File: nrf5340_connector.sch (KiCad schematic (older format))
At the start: 0 parts

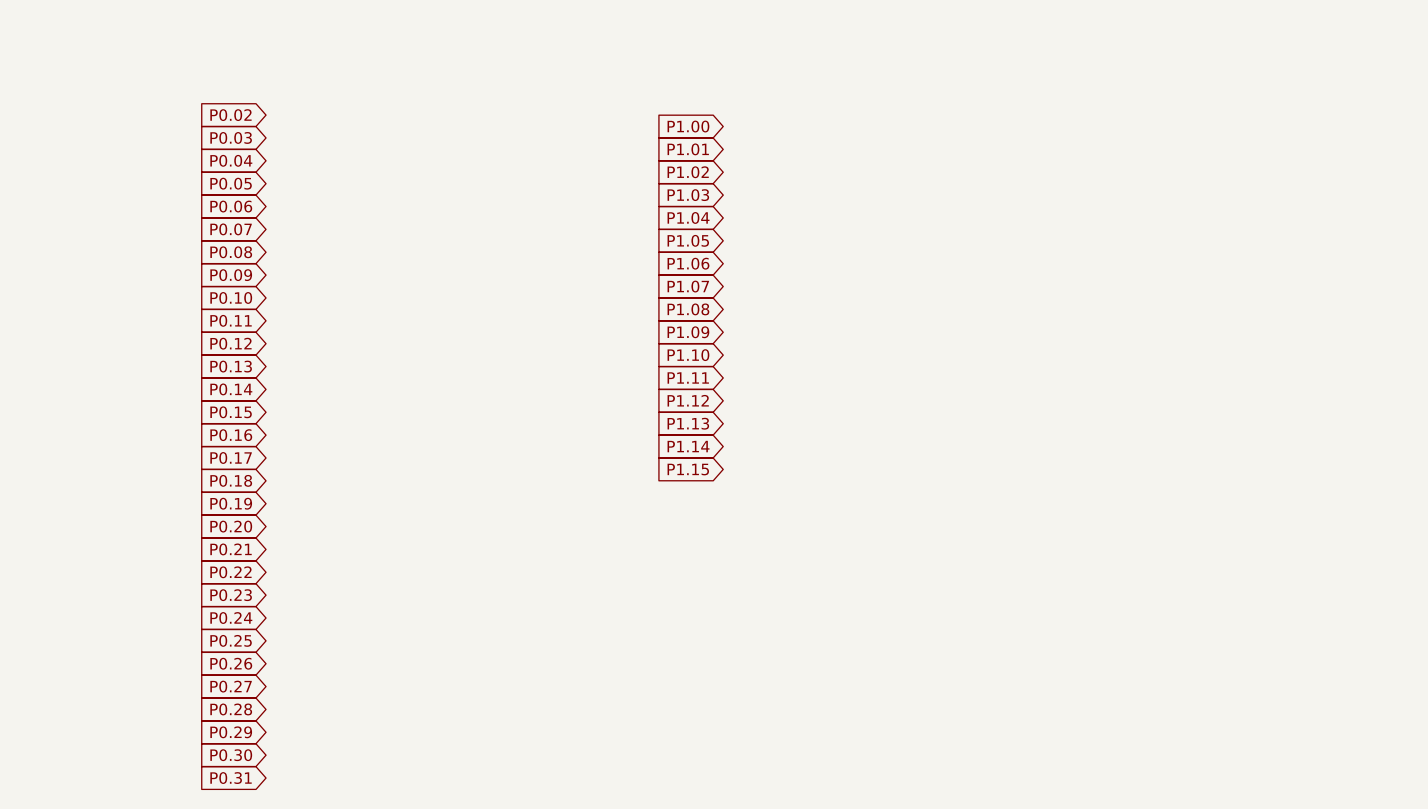
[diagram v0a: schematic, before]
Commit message: first rev pcb without impedance matching
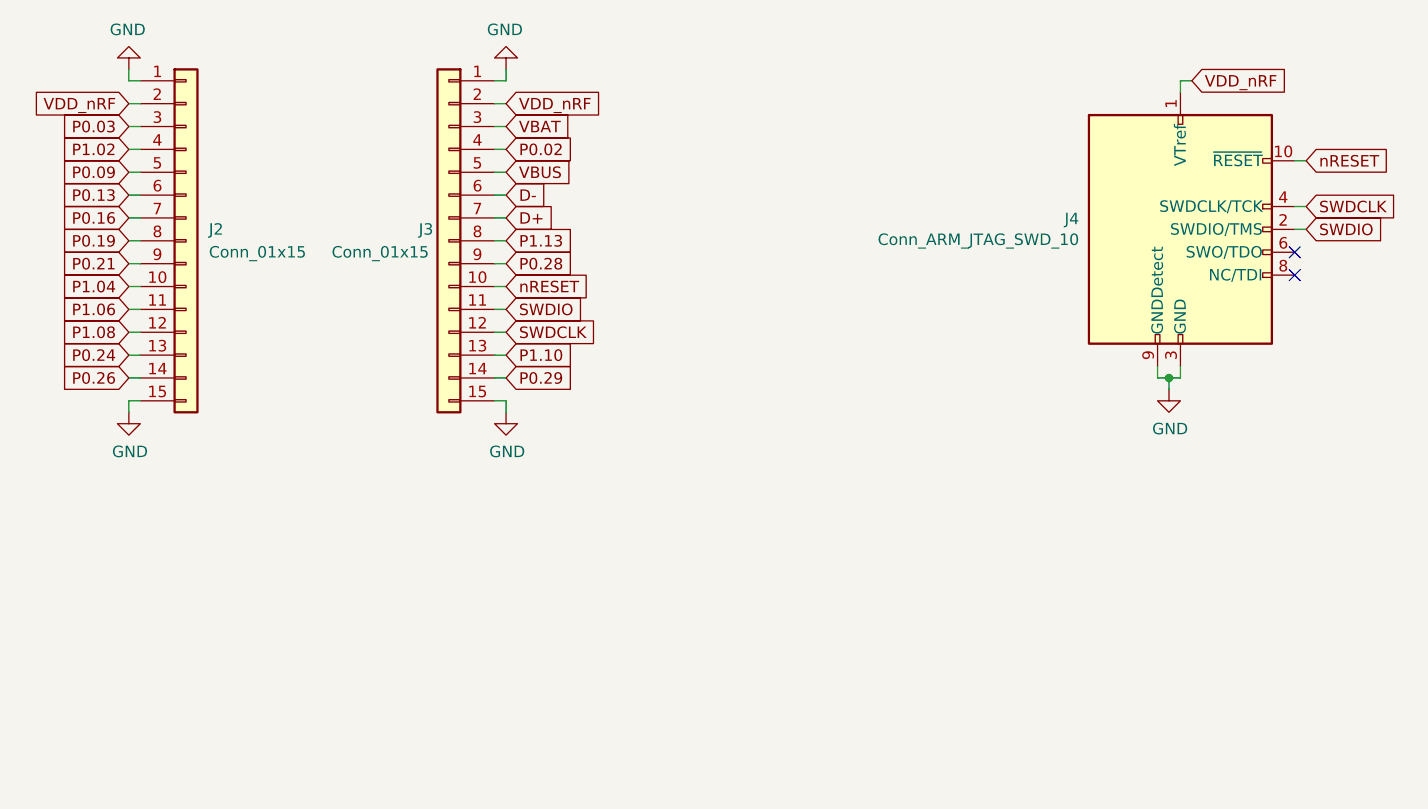
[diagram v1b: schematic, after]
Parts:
- added J2, J3: Conn_01x15, Connector_PinHeader_1.27mm:PinHeader_1x15_P1.27mm_Vertical, symbol Connector_Generic:Conn_01x15
- added J4: Conn_ARM_JTAG_SWD_10, Connector_PinHeader_1.27mm:PinHeader_2x05_P1.27mm_Vertical_SMD, symbol Connector:Conn_ARM_JTAG_SWD_10
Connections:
- net P0.02: now also J3.4 (Pin_4)
- net P0.03: now also J2.3 (Pin_3)
- net P0.09: now also J2.5 (Pin_5)
- net P0.13: now also J2.6 (Pin_6)
- net P0.16: now also J2.7 (Pin_7)
- net P0.19: now also J2.8 (Pin_8)
- net P0.21: now also J2.9 (Pin_9)
- net P0.24: now also J2.13 (Pin_13)
- net P0.26: now also J2.14 (Pin_14)
- net P0.28: now also J3.9 (Pin_9)
- net P0.29: now also J3.14 (Pin_14)
- net P1.02: now also J2.4 (Pin_4)
- net P1.04: now also J2.10 (Pin_10)
- net P1.06: now also J2.11 (Pin_11)
- net P1.08: now also J2.12 (Pin_12)
- net P1.10: now also J3.13 (Pin_13)
- net P1.13: now also J3.8 (Pin_8)
- new net D+: J3.7 (Pin_7)
- new net D-: J3.6 (Pin_6)
- new net GND: J2.1 (Pin_1), J2.15 (Pin_15), J3.1 (Pin_1), J3.15 (Pin_15), J4.3 (GND), J4.5 (GND), J4.9 (GNDDetect)
- new net SWDCLK: J3.12 (Pin_12), J4.4 (SWDCLK/TCK)
- new net SWDIO: J3.11 (Pin_11), J4.2 (SWDIO/TMS)
- new net VBAT: J3.3 (Pin_3)
- new net VBUS: J3.5 (Pin_5)
- new net VDD_nRF: J2.2 (Pin_2), J3.2 (Pin_2), J4.1 (VTref)
- new net nRESET: J3.10 (Pin_10), J4.10 (~RESET~)
- no-connect marks 0 -> 2

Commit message: fix traces underneath nrf gnd pad and VDD_HV
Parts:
- renumbered J4 to J?, J2 to J?, J3 to J?
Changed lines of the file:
@@
 EESchema Schematic File Version 4
+LIBS:nrf5340_module-cache
 EELAYER 30 0
 EELAYER END
@@
 P1.13
 $Comp
-L Connector:Conn_ARM_JTAG_SWD_10 J4
+L Connector:Conn_ARM_JTAG_SWD_10 J?
 U 1 1 5E0665C6
 P 5500 1400
-F 0 "J4" H 5057 1446 50  0000 R CNN
+F 0 "J?" H 5057 1446 50  0000 R CNN
 F 1 "Conn_ARM_JTAG_SWD_10" H 5057 1355 50  0000 R CNN
 F 2 "Connector_PinHeader_1.27mm:PinHeader_2x05_P1.27mm_Vertical_SMD" H 5500 1400 50  0001 C CNN
@@
 VDD_nRF
 $Comp
-L power:GND #PWR0123
+L power:GND #PWR?
 U 1 1 5E077D9A
 P 900 700
-F 0 "#PWR0123" H 900 450 50  0001 C CNN
+F 0 "#PWR?" H 900 450 50  0001 C CNN
 F 1 "GND" H 905 527 50  0000 C CNN
 F 2 "" H 900 700 50  0001 C CNN
@@
 $EndComp
 $Comp
-L power:GND #PWR0124
+L power:GND #PWR?
 U 1 1 5E0780C3
 P 900 2200
-F 0 "#PWR0124" H 900 1950 50  0001 C CNN
+F 0 "#PWR?" H 900 1950 50  0001 C CNN
 F 1 "GND" H 905 2027 50  0000 C CNN
 F 2 "" H 900 2200 50  0001 C CNN
@@
 $EndComp
 $Comp
-L power:GND #PWR0127
+L power:GND #PWR?
 U 1 1 5E078950
 P 2550 2200
-F 0 "#PWR0127" H 2550 1950 50  0001 C CNN
+F 0 "#PWR?" H 2550 1950 50  0001 C CNN
 F 1 "GND" H 2555 2027 50  0000 C CNN
 F 2 "" H 2550 2200 50  0001 C CNN
@@
 $EndComp
 $Comp
-L power:GND #PWR0128
+L power:GND #PWR?
 U 1 1 5E07908A
 P 2550 700
-F 0 "#PWR0128" H 2550 450 50  0001 C CNN
+F 0 "#PWR?" H 2550 450 50  0001 C CNN
 F 1 "GND" H 2555 527 50  0000 C CNN
 F 2 "" H 2550 700 50  0001 C CNN
@@
 $EndComp
 $Comp
-L power:GND #PWR0129
+L power:GND #PWR?
 U 1 1 5E07B32C
 P 5450 2100
-F 0 "#PWR0129" H 5450 1850 50  0001 C CNN
+F 0 "#PWR?" H 5450 1850 50  0001 C CNN
 F 1 "GND" H 5455 1927 50  0000 C CNN
 F 2 "" H 5450 2100 50  0001 C CNN
@@
 	900  700  900  750
 $Comp
-L Connector_Generic:Conn_01x15 J2
+L Connector_Generic:Conn_01x15 J?
 U 1 1 5E152486
 P 1150 1450
-F 0 "J2" H 1250 1500 50  0000 L CNN
+F 0 "J?" H 1250 1500 50  0000 L CNN
 F 1 "Conn_01x15" H 1250 1400 50  0000 L CNN
 F 2 "Connector_PinHeader_1.27mm:PinHeader_1x15_P1.27mm_Vertical" H 1150 1450 50  0001 C CNN
@@
 	950  850  900  850
 $Comp
-L Connector_Generic:Conn_01x15 J3
+L Connector_Generic:Conn_01x15 J?
 U 1 1 5E15CBB6
 P 2300 1450
-F 0 "J3" H 2400 1500 50  0000 C CNN
+F 0 "J?" H 2400 1500 50  0000 C CNN
 F 1 "Conn_01x15" H 2600 1400 50  0000 C CNN
 F 2 "Connector_PinHeader_1.27mm:PinHeader_1x15_P1.27mm_Vertical" H 2300 1450 50  0001 C CNN

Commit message: fix vdd_hv
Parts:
- gave numbers to parts that had none: 3
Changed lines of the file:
@@
 P1.13
 $Comp
-L Connector:Conn_ARM_JTAG_SWD_10 J?
+L Connector:Conn_ARM_JTAG_SWD_10 J4
 U 1 1 5E0665C6
 P 5500 1400
-F 0 "J?" H 5057 1446 50  0000 R CNN
+F 0 "J4" H 5057 1446 50  0000 R CNN
 F 1 "Conn_ARM_JTAG_SWD_10" H 5057 1355 50  0000 R CNN
 F 2 "Connector_PinHeader_1.27mm:PinHeader_2x05_P1.27mm_Vertical_SMD" H 5500 1400 50  0001 C CNN
@@
 VDD_nRF
 $Comp
-L power:GND #PWR?
+L power:GND #PWR0123
 U 1 1 5E077D9A
 P 900 700
-F 0 "#PWR?" H 900 450 50  0001 C CNN
+F 0 "#PWR0123" H 900 450 50  0001 C CNN
 F 1 "GND" H 905 527 50  0000 C CNN
 F 2 "" H 900 700 50  0001 C CNN
@@
 $EndComp
 $Comp
-L power:GND #PWR?
+L power:GND #PWR0124
 U 1 1 5E0780C3
 P 900 2200
-F 0 "#PWR?" H 900 1950 50  0001 C CNN
+F 0 "#PWR0124" H 900 1950 50  0001 C CNN
 F 1 "GND" H 905 2027 50  0000 C CNN
 F 2 "" H 900 2200 50  0001 C CNN
@@
 $EndComp
 $Comp
-L power:GND #PWR?
+L power:GND #PWR0127
 U 1 1 5E078950
 P 2550 2200
-F 0 "#PWR?" H 2550 1950 50  0001 C CNN
+F 0 "#PWR0127" H 2550 1950 50  0001 C CNN
 F 1 "GND" H 2555 2027 50  0000 C CNN
 F 2 "" H 2550 2200 50  0001 C CNN
@@
 $EndComp
 $Comp
-L power:GND #PWR?
+L power:GND #PWR0128
 U 1 1 5E07908A
 P 2550 700
-F 0 "#PWR?" H 2550 450 50  0001 C CNN
+F 0 "#PWR0128" H 2550 450 50  0001 C CNN
 F 1 "GND" H 2555 527 50  0000 C CNN
 F 2 "" H 2550 700 50  0001 C CNN
@@
 $EndComp
 $Comp
-L power:GND #PWR?
+L power:GND #PWR0129
 U 1 1 5E07B32C
 P 5450 2100
-F 0 "#PWR?" H 5450 1850 50  0001 C CNN
+F 0 "#PWR0129" H 5450 1850 50  0001 C CNN
 F 1 "GND" H 5455 1927 50  0000 C CNN
 F 2 "" H 5450 2100 50  0001 C CNN
@@
 	900  700  900  750
 $Comp
-L Connector_Generic:Conn_01x15 J?
+L Connector_Generic:Conn_01x15 J2
 U 1 1 5E152486
 P 1150 1450
-F 0 "J?" H 1250 1500 50  0000 L CNN
+F 0 "J2" H 1250 1500 50  0000 L CNN
 F 1 "Conn_01x15" H 1250 1400 50  0000 L CNN
 F 2 "Connector_PinHeader_1.27mm:PinHeader_1x15_P1.27mm_Vertical" H 1150 1450 50  0001 C CNN
@@
 	950  850  900  850
 $Comp
-L Connector_Generic:Conn_01x15 J?
+L Connector_Generic:Conn_01x15 J3
 U 1 1 5E15CBB6
 P 2300 1450
-F 0 "J?" H 2400 1500 50  0000 C CNN
+F 0 "J3" H 2400 1500 50  0000 C CNN
 F 1 "Conn_01x15" H 2600 1400 50  0000 C CNN
 F 2 "Connector_PinHeader_1.27mm:PinHeader_1x15_P1.27mm_Vertical" H 2300 1450 50  0001 C CNN

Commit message: fix vddh stuff
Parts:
- renumbered J4 to J?, J2 to J?, J3 to J?
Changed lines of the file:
@@
 $Descr A4 11693 8268
 encoding utf-8
-Sheet 2 3
+Sheet 6 7
 Title ""
 Date ""
@@
 P1.13
 $Comp
-L Connector:Conn_ARM_JTAG_SWD_10 J4
+L Connector:Conn_ARM_JTAG_SWD_10 J?
 U 1 1 5E0665C6
 P 5500 1400
-F 0 "J4" H 5057 1446 50  0000 R CNN
+F 0 "J?" H 5057 1446 50  0000 R CNN
 F 1 "Conn_ARM_JTAG_SWD_10" H 5057 1355 50  0000 R CNN
 F 2 "Connector_PinHeader_1.27mm:PinHeader_2x05_P1.27mm_Vertical_SMD" H 5500 1400 50  0001 C CNN
@@
 VDD_nRF
 $Comp
-L power:GND #PWR0123
+L power:GND #PWR?
 U 1 1 5E077D9A
 P 900 700
-F 0 "#PWR0123" H 900 450 50  0001 C CNN
+F 0 "#PWR?" H 900 450 50  0001 C CNN
 F 1 "GND" H 905 527 50  0000 C CNN
 F 2 "" H 900 700 50  0001 C CNN
@@
 $EndComp
 $Comp
-L power:GND #PWR0124
+L power:GND #PWR?
 U 1 1 5E0780C3
 P 900 2200
-F 0 "#PWR0124" H 900 1950 50  0001 C CNN
+F 0 "#PWR?" H 900 1950 50  0001 C CNN
 F 1 "GND" H 905 2027 50  0000 C CNN
 F 2 "" H 900 2200 50  0001 C CNN
@@
 $EndComp
 $Comp
-L power:GND #PWR0127
+L power:GND #PWR?
 U 1 1 5E078950
 P 2550 2200
-F 0 "#PWR0127" H 2550 1950 50  0001 C CNN
+F 0 "#PWR?" H 2550 1950 50  0001 C CNN
 F 1 "GND" H 2555 2027 50  0000 C CNN
 F 2 "" H 2550 2200 50  0001 C CNN
@@
 $EndComp
 $Comp
-L power:GND #PWR0128
+L power:GND #PWR?
 U 1 1 5E07908A
 P 2550 700
-F 0 "#PWR0128" H 2550 450 50  0001 C CNN
+F 0 "#PWR?" H 2550 450 50  0001 C CNN
 F 1 "GND" H 2555 527 50  0000 C CNN
 F 2 "" H 2550 700 50  0001 C CNN
@@
 $EndComp
 $Comp
-L power:GND #PWR0129
+L power:GND #PWR?
 U 1 1 5E07B32C
 P 5450 2100
-F 0 "#PWR0129" H 5450 1850 50  0001 C CNN
+F 0 "#PWR?" H 5450 1850 50  0001 C CNN
 F 1 "GND" H 5455 1927 50  0000 C CNN
 F 2 "" H 5450 2100 50  0001 C CNN
@@
 	900  700  900  750
 $Comp
-L Connector_Generic:Conn_01x15 J2
+L Connector_Generic:Conn_01x15 J?
 U 1 1 5E152486
 P 1150 1450
-F 0 "J2" H 1250 1500 50  0000 L CNN
+F 0 "J?" H 1250 1500 50  0000 L CNN
 F 1 "Conn_01x15" H 1250 1400 50  0000 L CNN
 F 2 "Connector_PinHeader_1.27mm:PinHeader_1x15_P1.27mm_Vertical" H 1150 1450 50  0001 C CNN
@@
 	950  850  900  850
 $Comp
-L Connector_Generic:Conn_01x15 J3
+L Connector_Generic:Conn_01x15 J?
 U 1 1 5E15CBB6
 P 2300 1450
-F 0 "J3" H 2400 1500 50  0000 C CNN
+F 0 "J?" H 2400 1500 50  0000 C CNN
 F 1 "Conn_01x15" H 2600 1400 50  0000 C CNN
 F 2 "Connector_PinHeader_1.27mm:PinHeader_1x15_P1.27mm_Vertical" H 2300 1450 50  0001 C CNN

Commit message: update
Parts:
- gave numbers to parts that had none: 3
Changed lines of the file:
@@
 EESchema Schematic File Version 4
-LIBS:nrf5340_module-cache
 EELAYER 30 0
 EELAYER END
 $Descr A4 11693 8268
 encoding utf-8
-Sheet 6 7
+Sheet 2 3
 Title ""
 Date ""
-Rev ""
+Rev "1.0"
 Comp ""
 Comment1 ""
@@
 P1.13
 $Comp
-L Connector:Conn_ARM_JTAG_SWD_10 J?
+L Connector:Conn_ARM_JTAG_SWD_10 J4
 U 1 1 5E0665C6
 P 5500 1400
-F 0 "J?" H 5057 1446 50  0000 R CNN
+F 0 "J4" H 5057 1446 50  0000 R CNN
 F 1 "Conn_ARM_JTAG_SWD_10" H 5057 1355 50  0000 R CNN
 F 2 "Connector_PinHeader_1.27mm:PinHeader_2x05_P1.27mm_Vertical_SMD" H 5500 1400 50  0001 C CNN
@@
 VDD_nRF
 $Comp
-L power:GND #PWR?
+L power:GND #PWR09
 U 1 1 5E077D9A
 P 900 700
-F 0 "#PWR?" H 900 450 50  0001 C CNN
+F 0 "#PWR09" H 900 450 50  0001 C CNN
 F 1 "GND" H 905 527 50  0000 C CNN
 F 2 "" H 900 700 50  0001 C CNN
@@
 $EndComp
 $Comp
-L power:GND #PWR?
+L power:GND #PWR010
 U 1 1 5E0780C3
 P 900 2200
-F 0 "#PWR?" H 900 1950 50  0001 C CNN
+F 0 "#PWR010" H 900 1950 50  0001 C CNN
 F 1 "GND" H 905 2027 50  0000 C CNN
 F 2 "" H 900 2200 50  0001 C CNN
@@
 $EndComp
 $Comp
-L power:GND #PWR?
+L power:GND #PWR012
 U 1 1 5E078950
 P 2550 2200
-F 0 "#PWR?" H 2550 1950 50  0001 C CNN
+F 0 "#PWR012" H 2550 1950 50  0001 C CNN
 F 1 "GND" H 2555 2027 50  0000 C CNN
 F 2 "" H 2550 2200 50  0001 C CNN
@@
 $EndComp
 $Comp
-L power:GND #PWR?
+L power:GND #PWR011
 U 1 1 5E07908A
 P 2550 700
-F 0 "#PWR?" H 2550 450 50  0001 C CNN
+F 0 "#PWR011" H 2550 450 50  0001 C CNN
 F 1 "GND" H 2555 527 50  0000 C CNN
 F 2 "" H 2550 700 50  0001 C CNN
@@
 $EndComp
 $Comp
-L power:GND #PWR?
+L power:GND #PWR013
 U 1 1 5E07B32C
 P 5450 2100
-F 0 "#PWR?" H 5450 1850 50  0001 C CNN
+F 0 "#PWR013" H 5450 1850 50  0001 C CNN
 F 1 "GND" H 5455 1927 50  0000 C CNN
 F 2 "" H 5450 2100 50  0001 C CNN
@@
 	900  700  900  750
 $Comp
-L Connector_Generic:Conn_01x15 J?
+L Connector_Generic:Conn_01x15 J2
 U 1 1 5E152486
 P 1150 1450
-F 0 "J?" H 1250 1500 50  0000 L CNN
+F 0 "J2" H 1250 1500 50  0000 L CNN
 F 1 "Conn_01x15" H 1250 1400 50  0000 L CNN
 F 2 "Connector_PinHeader_1.27mm:PinHeader_1x15_P1.27mm_Vertical" H 1150 1450 50  0001 C CNN
@@
 	950  850  900  850
 $Comp
-L Connector_Generic:Conn_01x15 J?
+L Connector_Generic:Conn_01x15 J3
 U 1 1 5E15CBB6
 P 2300 1450
-F 0 "J?" H 2400 1500 50  0000 C CNN
+F 0 "J3" H 2400 1500 50  0000 C CNN
 F 1 "Conn_01x15" H 2600 1400 50  0000 C CNN
 F 2 "Connector_PinHeader_1.27mm:PinHeader_1x15_P1.27mm_Vertical" H 2300 1450 50  0001 C CNN
